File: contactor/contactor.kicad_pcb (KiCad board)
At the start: 2 copper layers, 43.3 x 67 mm, 27 parts, among them J1 Screw_Terminal_01x01, J2 Screw_Terminal_01x01, J3 Screw_Terminal_01x01, J4 Screw_Terminal_01x01, J5 Screw_Terminal_01x01, J6 Screw_Terminal_01x01, J7 Screw_Terminal_01x01, Q1 Q_NMOS_DGS, U1 74LS21

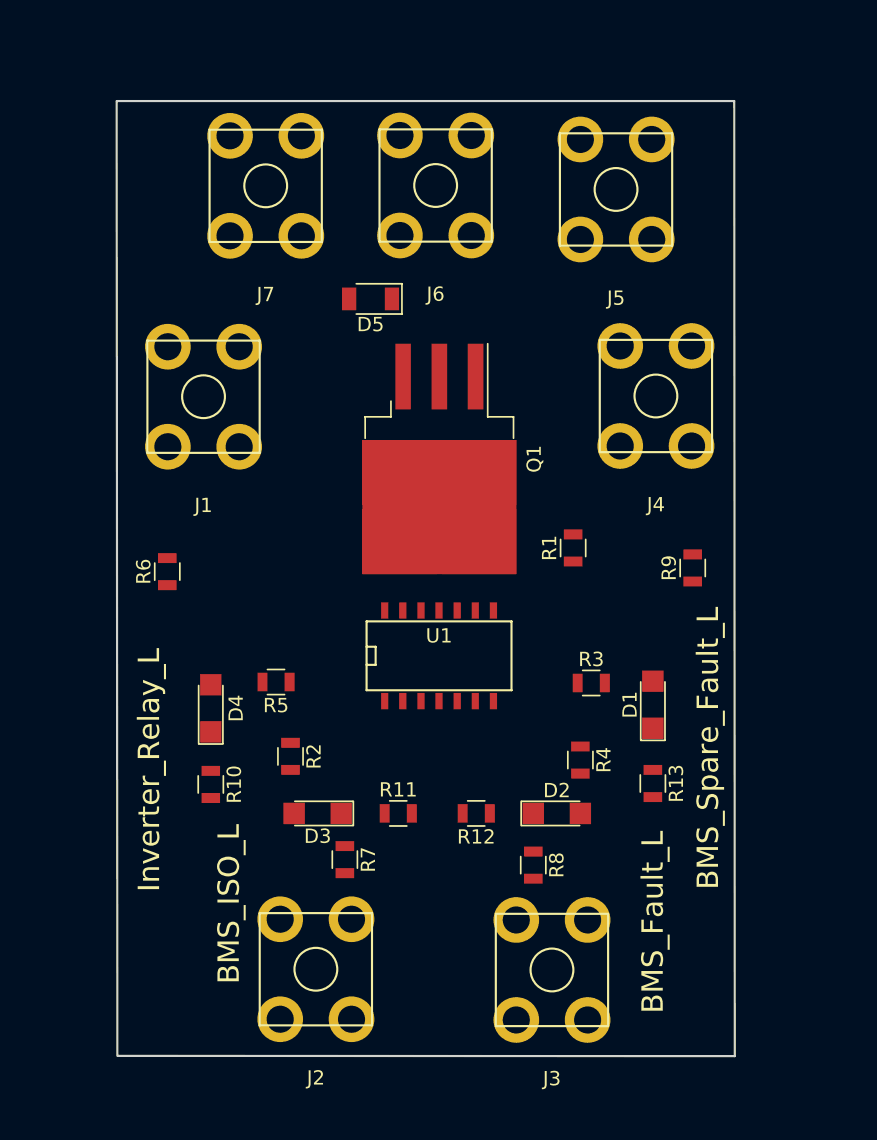
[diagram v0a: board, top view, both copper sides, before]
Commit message: Routing almost done, need to connect 12V traces
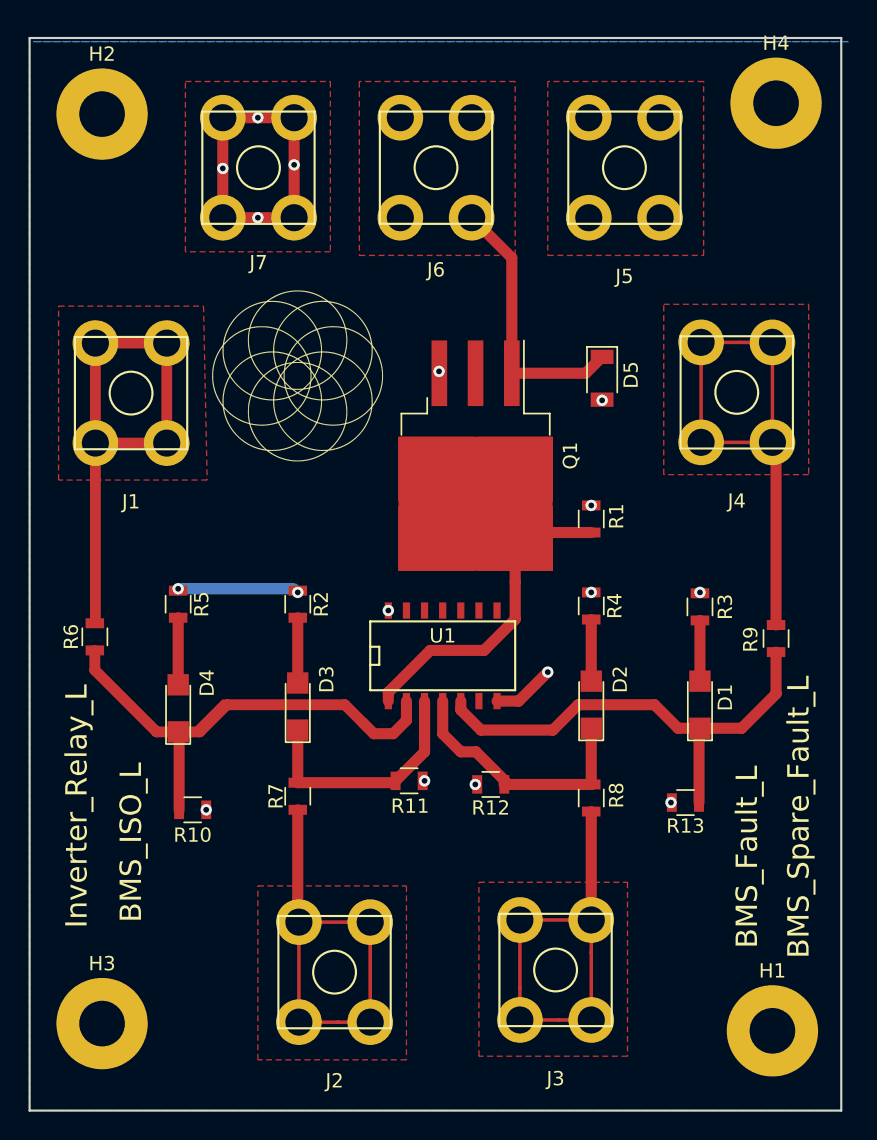
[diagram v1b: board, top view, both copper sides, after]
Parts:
- added G***: LOGO, hyperCustom:ParadigmLogo_0_5x0_5, F.Cu at (84.1, 65.5)
- added H1: MountingHole_Pad, Mounting_Holes:MountingHole_3.2mm_M3_Pad, F.Cu at (117.3, 111.5)
- added H2: MountingHole_Pad, Mounting_Holes:MountingHole_3.2mm_M3_Pad, F.Cu at (70.4, 47.2)
- added H3: MountingHole_Pad, Mounting_Holes:MountingHole_3.2mm_M3_Pad, F.Cu at (70.4, 111.0)
- added H4: MountingHole_Pad, Mounting_Holes:MountingHole_3.2mm_M3_Pad, F.Cu at (117.6, 46.5)
- moved D5 17.2 mm to (105.4, 65.8), turned to 270 degrees
- moved R4 10.8 mm to (104.6, 81.7)
- moved R2 10.7 mm to (84.1, 81.6)
- moved R3 9.30 mm to (112.3, 81.8), turned to 270 degrees
- moved R5 8.76 mm to (75.7, 81.6), turned to 270 degrees
- moved D2 7.99 mm to (104.6, 88.6), turned to 90 degrees
- moved R9 7.66 mm to (117.6, 84.0)
- moved D3 7.62 mm to (84.1, 88.8), turned to 90 degrees
- moved R6 6.83 mm to (69.8, 83.9)
- moved R8 6.22 mm to (104.6, 95.2)
- moved J4 5.67 mm to (114.8, 66.8)
- moved R7 5.53 mm to (84.1, 95.1)
- moved J1 5.09 mm to (72.4, 66.8)
- moved D1 3.30 mm to (112.3, 88.6)
- moved R13 2.65 mm to (111.3, 95.5), turned to 180 degrees
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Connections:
- U1 pad 1: /Inverter_Relay_L -> Net-(Q1-Pad2)
- U1 pad 14: (no net) -> +12V
- U1 pad 2: /BMS_ISO_L -> /Inverter_Relay_L
- U1 pad 3: (no net) -> /BMS_ISO_L
- U1 pad 6: Net-(Q1-Pad2) -> (no net)
- U1 pad 7: (no net) -> GND
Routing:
- net /Inverter_Relay_L: track 0.00 -> 38.2 mm
- net Net-(J4-Pad1): track 0.00 -> 36.9 mm
- net Net-(J1-Pad1): track 0.00 -> 36.8 mm
- net /BMS_Spare_Fault_L: track 0.00 -> 34.3 mm
- net Net-(J3-Pad1): track 0.00 -> 33.9 mm
- net Net-(J2-Pad1): track 0.00 -> 32.0 mm
- net Net-(Q1-Pad2): track 0.00 -> 30.3 mm
- net GND: track 0.00 -> 28.4 mm, vias 0 -> 11
- net Contactor-: track 0.00 -> 19.3 mm
- net /BMS_Fault_L: track 0.00 -> 18.6 mm
- net /BMS_ISO_L: track 0.00 -> 17.3 mm
- net +12V: track 0.00 -> 8.54 mm, vias 0 -> 6
- net Net-(D4-Pad2): track 0.00 -> 4.70 mm
- net Net-(D3-Pad2): track 0.00 -> 4.57 mm
- net Net-(D2-Pad2): track 0.00 -> 4.32 mm
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- added copper zone on F.Cu, net +12V
- added copper zone on F.Cu, net Contactor-
- added copper zone on B.Cu, net GND
- added copper zone on F.Cu, net GND
- added copper zone on F.Cu, net Net-(J1-Pad1)
- added copper zone on F.Cu, net Net-(J2-Pad1)
- added copper zone on F.Cu, net Net-(J3-Pad1)
- added copper zone on F.Cu, net Net-(J4-Pad1)
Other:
- board size 43.3 x 67 mm -> 56.9 x 75.2 mm
- net class Default: trace_width 0.25 -> 0.78

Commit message: Routing done. Ready for review
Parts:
- moved D5 1.81 mm to (103.9, 64.8)
- moved Q1 1.15 mm to (96.5, 70.0)
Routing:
- net +12V: track 8.54 -> 71.8 mm
- net Contactor-: track 19.3 -> 18.0 mm
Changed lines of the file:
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@@
     (thickness 1.6)
     (drawings 8)
-    (tracks 130)
+    (tracks 150)
     (zones 0)
     (modules 32)
@@
   )
   (module Diodes_SMD:D_1206 (layer F.Cu)
-    (at 105.41 65.762 270)
+    (at 103.886 64.794 270)
     (descr "Diode SMD 1206, reflow soldering http://datasheets.avx.com/schottky.pdf")
     (tags "Diode 1206")
     (attr smd)
-    (fp_text reference D5 (at -0.23 -2.032 270) (layer F.SilkS)
+    (fp_text reference D5 (at 3.532 -0.254 270) (layer F.SilkS)
       (effects (font (size 1 1) (thickness 0.15)))
     )
@@
   )
   (module TO_SOT_Packages_SMD:TO-263-3_TabPin2 (layer F.Cu)
-    (at 96.539 71.186 270)
+    (at 96.539 70.037 270)
     (descr "TO-263 / D2PAK / DDPAK SMD package, http://www.infineon.com/cms/en/product/packages/PG-TO263/PG-TO263-3-1/")
     (tags "D2PAK DDPAK TO-263 D2PAK-3 TO-263-3 SOT-404")
     (attr smd)
-    (fp_text reference Q1 (at 0 -6.65 270) (layer F.SilkS)
+    (fp_text reference Q1 (at -9.21 1.797) (layer F.SilkS)
       (effects (font (size 1 1) (thickness 0.15)))
     )
@@
   (segment (start 97.668 76.576) (end 97.028 77.216) (width 0.25) (layer F.Cu) (net 5))
   (segment (start 96.774 88.392) (end 96.774 88.0745) (width 0.25) (layer F.Cu) (net 0))
+  (via (at 103.886 66.294) (size 0.8) (drill 0.4) (layers F.Cu B.Cu) (net 3))
   (via (at 112.268 80.772) (size 0.8) (drill 0.4) (layers F.Cu B.Cu) (net 10))
   (via (at 84.074 80.772) (size 0.8) (drill 0.4) (layers F.Cu B.Cu) (net 10))
@@
   (segment (start 75.692 87.25) (end 75.692 82.55) (width 0.78) (layer F.Cu) (net 2))
   (via (at 93.98 65.278) (size 0.8) (drill 0.4) (layers F.Cu B.Cu) (net 3))
-  (via (at 105.41 67.31) (size 0.8) (drill 0.4) (layers F.Cu B.Cu) (net 3))
   (via (at 77.658 96.012) (size 0.8) (drill 0.4) (layers F.Cu B.Cu) (net 3))
   (via (at 92.964 93.98) (size 0.8) (drill 0.4) (layers F.Cu B.Cu) (net 3))
@@
   (via (at 101.6 86.36) (size 0.8) (drill 0.4) (layers F.Cu B.Cu) (net 3))
   (segment (start 99.568 88.392) (end 101.6 86.36) (width 0.78) (layer F.Cu) (net 3))
-  (segment (start 98.044 88.392) (end 99.568 88.392) (width 0.78) (layer F.Cu) (net 3))
   (segment (start 78.82 54.508) (end 78.82 51.054) (width 0.78) (layer F.Cu) (net 3))
   (segment (start 78.82 47.498) (end 81.28 47.498) (width 0.78) (layer F.Cu) (net 3))
@@
   (segment (start 81.28 54.508) (end 78.82 54.508) (width 0.78) (layer F.Cu) (net 3))
   (via (at 81.28 54.508) (size 0.8) (drill 0.4) (layers F.Cu B.Cu) (net 3))
+  (segment (start 99.568 88.392) (end 98.298 88.392) (width 0.78) (layer F.Cu) (net 3))
   (segment (start 99.079 57.321) (end 96.266 54.508) (width 0.78) (layer F.Cu) (net 4))
-  (segment (start 99.079 65.411) (end 99.079 57.321) (width 0.78) (layer F.Cu) (net 4))
-  (segment (start 104.261 65.411) (end 105.41 64.262) (width 0.78) (layer F.Cu) (net 4))
-  (segment (start 99.079 65.411) (end 104.261 65.411) (width 0.78) (layer F.Cu) (net 4))
+  (segment (start 103.886 62.014) (end 102.578 60.706) (width 0.78) (layer F.Cu) (net 4))
+  (segment (start 102.578 60.706) (end 99.079 60.706) (width 0.78) (layer F.Cu) (net 4))
+  (segment (start 103.886 63.294) (end 103.886 62.014) (width 0.78) (layer F.Cu) (net 4))
+  (segment (start 99.079 60.706) (end 99.079 57.321) (width 0.78) (layer F.Cu) (net 4))
+  (segment (start 99.079 60.706) (end 99.079 64.262) (width 0.78) (layer F.Cu) (net 4))
   (segment (start 90.424 88.392) (end 90.424 88.0745) (width 0.25) (layer F.Cu) (net 5))
   (segment (start 97.239 74.561) (end 96.539 74.561) (width 0.25) (layer F.Cu) (net 5))
@@
   (via (at 104.648 74.676) (size 0.8) (drill 0.4) (layers F.Cu B.Cu) (net 10))
   (segment (start 75.692 80.518) (end 83.82 80.518) (width 0.78) (layer B.Cu) (net 10))
+  (segment (start 89.154 80.772) (end 90.424 82.042) (width 0.78) (layer B.Cu) (net 10))
+  (segment (start 84.074 80.772) (end 89.154 80.772) (width 0.78) (layer B.Cu) (net 10))
+  (segment (start 106.172 74.676) (end 112.268 80.772) (width 0.78) (layer B.Cu) (net 10))
+  (segment (start 104.648 74.676) (end 106.172 74.676) (width 0.78) (layer B.Cu) (net 10))
+  (segment (start 106.400001 58.696742) (end 106.400001 72.161999) (width 0.78) (layer B.Cu) (net 10))
+  (segment (start 104.474 56.770741) (end 106.400001 58.696742) (width 0.78) (layer B.Cu) (net 10))
+  (segment (start 104.474 54.508) (end 104.474 56.770741) (width 0.78) (layer B.Cu) (net 10))
+  (segment (start 106.400001 73.223999) (end 104.948 74.676) (width 0.78) (layer B.Cu) (net 10))
+  (segment (start 106.400001 72.161999) (end 106.400001 73.223999) (width 0.78) (layer B.Cu) (net 10))
+  (segment (start 104.348 80.772) (end 105.156 80.772) (width 0.78) (layer B.Cu) (net 10))
+  (segment (start 105.156 80.772) (end 112.268 80.772) (width 0.78) (layer B.Cu) (net 10))
+  (segment (start 104.648 80.772) (end 105.156 80.772) (width 0.78) (layer B.Cu) (net 10))
+  (segment (start 104.348 80.772) (end 104.648 80.772) (width 0.78) (layer B.Cu) (net 10))
+  (segment (start 103.124 80.772) (end 104.648 80.772) (width 0.78) (layer B.Cu) (net 10))
+  (segment (start 102.616 80.264) (end 103.124 80.772) (width 0.78) (layer B.Cu) (net 10))
+  (segment (start 90.8505 80.264) (end 102.616 80.264) (width 0.78) (layer B.Cu) (net 10))
+  (segment (start 90.424 80.6905) (end 90.8505 80.264) (width 0.78) (layer B.Cu) (net 10))
+  (segment (start 90.424 82.042) (end 90.424 80.6905) (width 0.78) (layer B.Cu) (net 10))
   (segment (start 112.268 86.996) (end 112.268 82.738) (width 0.78) (layer F.Cu) (net 11))
   (segment (start 84.074 82.55) (end 84.074 87.124) (width 0.78) (layer F.Cu) (net 12))
